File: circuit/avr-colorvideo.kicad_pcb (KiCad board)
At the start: 2 copper layers, 229.9 x 111.8 mm, 148 parts, among them J1 USB-B, J2 AVR-ISP-6, J3 RCA, J4 RCA, J5 SPI1, J6 SPI0, J7 ANALOG, J8 6P6C, J9 6P6C, K1 SW_Push, K10 SW_Push, K11 SW_Push, K12 SW_Push, K13 SW_Push, K14 SW_Push, K15 SW_Push, K16 SW_Push, K17 SW_Push, K18 SW_Push, K19 SW_Push, K2 SW_Push, K20 SW_Push, K21 SW_Push, K22 SW_Push, K23 SW_Push, K24 SW_Push, K25 SW_Push, K26 SW_Push, K27 SW_Push, K28 SW_Push, K29 SW_Push, K3 SW_Push, K30 SW_Push, K31 SW_Push, K32 SW_Push, K33 SW_Push, K34 SW_Push, K35 SW_Push, K36 SW_Push, K37 SW_Push, K38 SW_Push, K39 SW_Push, K4 SW_Push, K40 SW_Push, K41 SW_Push, K42 SW_Push, K43 SW_Push, K44 SW_Push, K45 SW_Push, K46 SW_Push, K47 SW_Push, K5 SW_Push, K6 SW_Push, K7 SW_Push, K8 SW_Push, K9 SW_Push, SW1 SW_Push, SW2 SPI1/ISP, U1 ATmega1284P-PU, U2 74HC157, U3 74HC157, U4 74HC166, U5 74HC166, U6 FT230XS, Y1 14.31818MHz

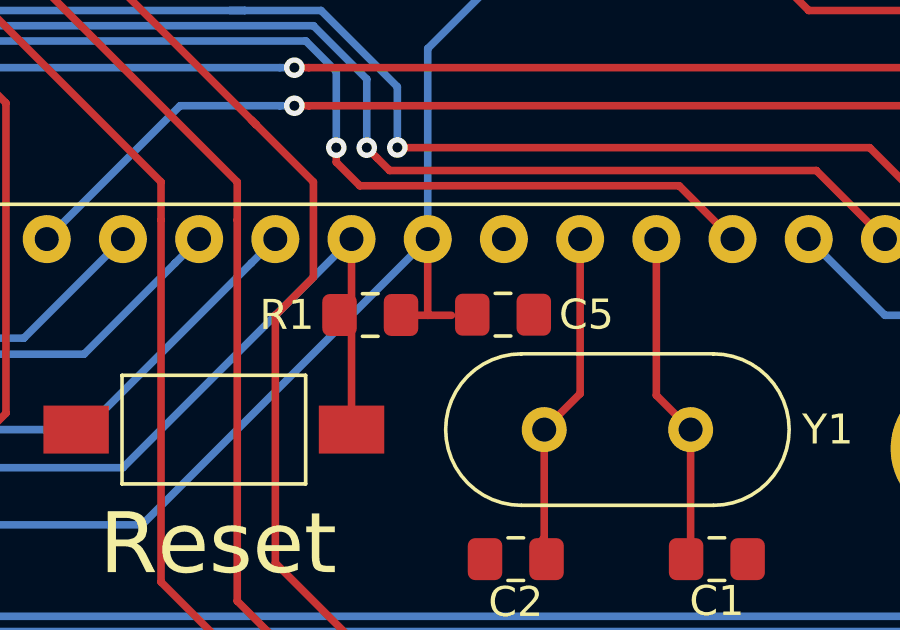
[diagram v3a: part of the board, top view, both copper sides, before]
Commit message: Fix unconnected pad, regenerate gerbers
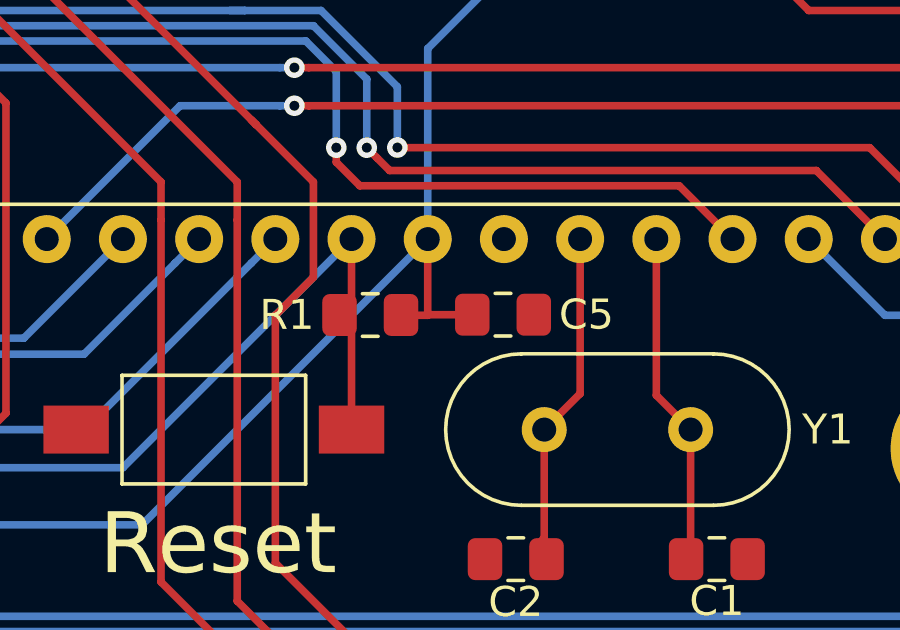
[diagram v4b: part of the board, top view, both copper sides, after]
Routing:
- net VCC: track 394.9 -> 395.6 mm
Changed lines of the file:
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@@
   (general
     (thickness 1.6)
-    (drawings 103)
-    (tracks 1490)
+    (drawings 105)
+    (tracks 1491)
     (zones 0)
     (modules 148)
@@
     )
   )
+  (dimension 111.76 (width 0.15) (layer F.SilkS)
+    (gr_text "111.760 mm" (at 256.45 78.74 270) (layer F.SilkS)
+      (effects (font (size 1 1) (thickness 0.15)))
+    )
+    (feature1 (pts (xy 252.7 134.62) (xy 255.736421 134.62)))
+    (feature2 (pts (xy 252.7 22.86) (xy 255.736421 22.86)))
+    (crossbar (pts (xy 255.15 22.86) (xy 255.15 134.62)))
+    (arrow1a (pts (xy 255.15 134.62) (xy 254.563579 133.493496)))
+    (arrow1b (pts (xy 255.15 134.62) (xy 255.736421 133.493496)))
+    (arrow2a (pts (xy 255.15 22.86) (xy 254.563579 23.986504)))
+    (arrow2b (pts (xy 255.15 22.86) (xy 255.736421 23.986504)))
+  )
+  (dimension 229.86 (width 0.15) (layer F.SilkS)
+    (gr_text "229.860 mm" (at 137.800219 139.634812 0.002492638105) (layer F.SilkS)
+      (effects (font (size 1 1) (thickness 0.15)))
+    )
+    (feature1 (pts (xy 252.73 134.61) (xy 252.730187 138.916233)))
+    (feature2 (pts (xy 22.87 134.62) (xy 22.870187 138.926233)))
+    (crossbar (pts (xy 22.870162 138.339812) (xy 252.730162 138.329812)))
+    (arrow1a (pts (xy 252.730162 138.329812) (xy 251.603684 138.916282)))
+    (arrow1b (pts (xy 252.730162 138.329812) (xy 251.603633 137.74344)))
+    (arrow2a (pts (xy 22.870162 138.339812) (xy 23.996691 138.926184)))
+    (arrow2b (pts (xy 22.870162 138.339812) (xy 23.99664 137.753342)))
+  )
   (gr_line (start 86.36 37.465) (end 85.725 38.1) (layer F.SilkS) (width 0.15))
   (gr_line (start 86.995 31.115) (end 86.36 31.75) (layer F.SilkS) (width 0.15))
@@
   (segment (start 134.62 34.29) (end 132.08 36.83) (width 0.254) (layer B.Cu) (net 4))
   (segment (start 132.08 45.72) (end 132.08 43.18) (width 0.254) (layer F.Cu) (net 4))
-  (segment (start 132.87 45.72) (end 132.08 45.72) (width 0.254) (layer F.Cu) (net 4))
   (segment (start 132.08 45.72) (end 131.29 45.72) (width 0.254) (layer F.Cu) (net 4))
   (segment (start 195.961 27.94) (end 196.215 27.686) (width 0.254) (layer F.Cu) (net 4))
@@
   (segment (start 134.62 25.515) (end 135.025 25.11) (width 0.254) (layer F.Cu) (net 4))
   (segment (start 134.62 27.94) (end 134.62 25.515) (width 0.254) (layer F.Cu) (net 4))
+  (segment (start 132.1 45.7) (end 133.565 45.7) (width 0.254) (layer F.Cu) (net 4))
+  (segment (start 132.08 45.72) (end 132.1 45.7) (width 0.254) (layer F.Cu) (net 4))
   (segment (start 106.68 50.8) (end 107.95 49.53) (width 0.254) (layer B.Cu) (net 5))
   (segment (start 123.660001 43.979999) (end 124.46 43.18) (width 0.254) (layer B.Cu) (net 5))
